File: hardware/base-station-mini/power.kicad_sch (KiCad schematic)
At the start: 28 parts, among them U2 TPS61023DRLR, U22 TPS22918DBVR, U9 TPS63020DSJR

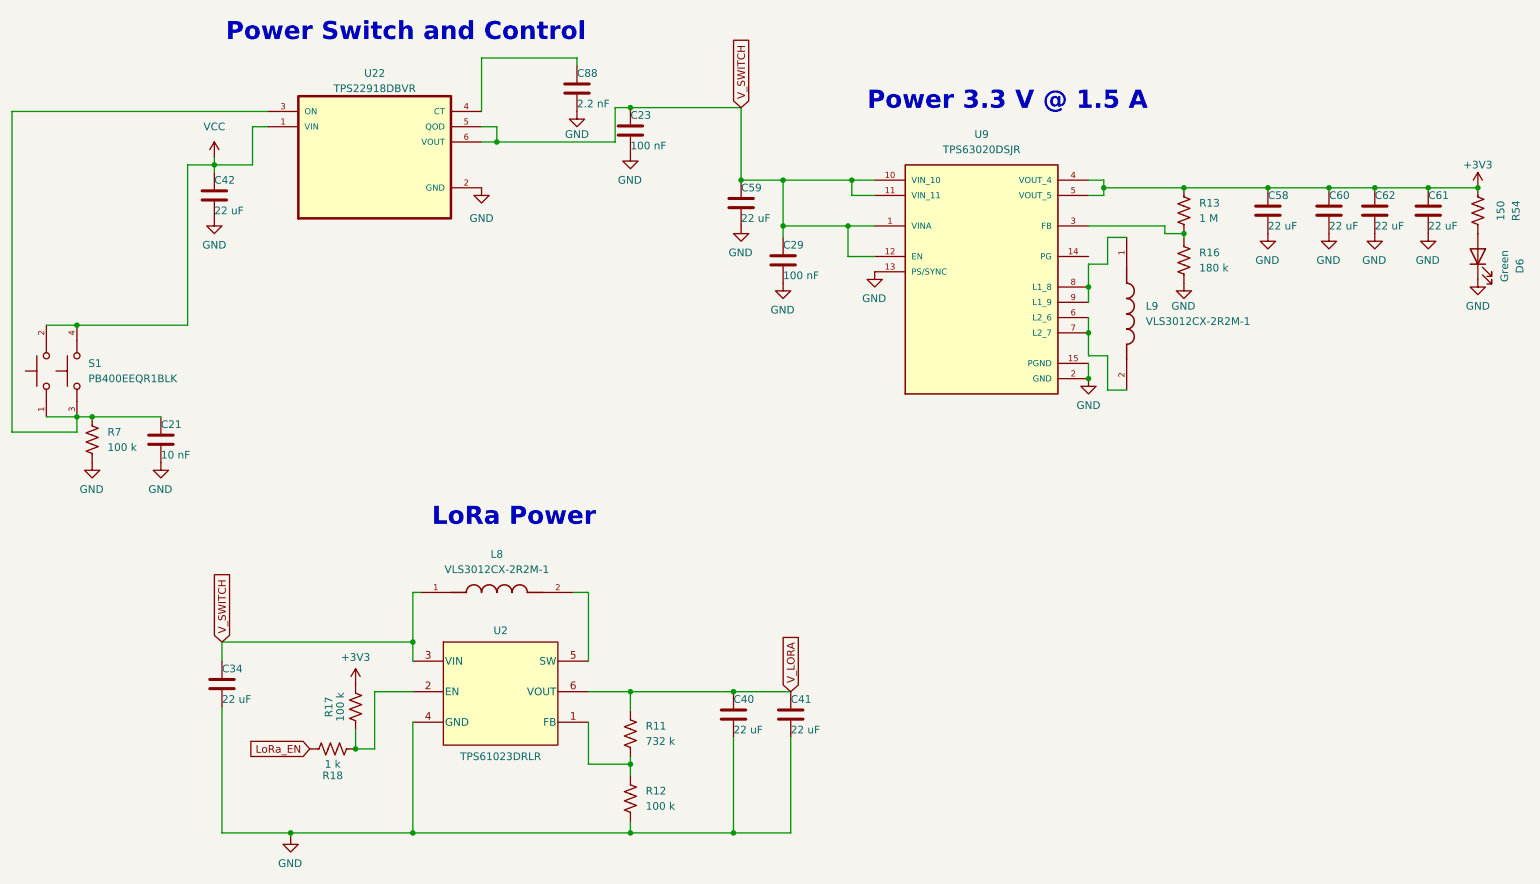
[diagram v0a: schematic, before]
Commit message: hardware: base-station-mini gains on-board LoRa, TPS63021, rev V1
Turns the fork into a reduced-feature ground station. "Mini" is fewer features,
not a smaller board -- the outline stays base-station's 30.27 x 90.50 mm.

RADIO. The E220-900MM22S (U16) is on-board on SPI, replacing the UART header
that fed an external lora-daughterboard. Eight ESP32 signals wired via the L_*
labels already placed on the module side; LoRa_TX/LoRa_RX/LoRa_EN were dangling
single-node stubs and their GPIOs went straight back into the radio bus.

All eight land on the same GPIOs as the fabbed lora-daughterboard -- SCK/17,
CS/18, MOSI/21, MISO/33, BUSY/34, RXEN/35, RST/38, DIO1/2 -- so the radio_board
firmware pin map applies unchanged. L_DI02 stays a module-local DIO2->TXEN loop,
so the SX1262 drives its own RF switch and spends no GPIO.

POWER. +3V3 had no source at all after the converters came out. Now a
fixed-output TPS63021 with FB tied to VOUT, matching base-station at V6. The 5 V
V_LORA boost stays deleted -- the on-board module runs off +3V3.

RF. J8 is new copper that exists on no other board. The feed was 0.20 mm, right
for a 0.1 mm prepreg but not for this stackup's real 0.2104 mm; it is now 0.36 mm
with a 0.15 mm coplanar gap, the value base-station's S7 derived for the same
JLCPCB JLC04161H-7628 stack. Net-(U16-ANT) was also missing from the RF netclass
-- the only RF net unique to this board was the one net not declared as RF -- so
it is added and the zones refilled.

ALSO. BT2 placed on B.Cu at base-station's exact coordinates, verified pad for
pad. external_charger.kicad_sch deleted rather than left orphaned; it held the
last copies of SDA_SENS, SCL_SENS, PosADC, MidADC and 25 dead symbols. Rev V1,
never fabbed. bom.csv regenerated -- it was 109 refs against a 78-ref schematic
and had never listed U16 or J8.

State: 0 schematic-parity issues, 0 unconnected, 25 DRC all silkscreen.
Reviewed in prefab-review-2026-08-12.md; three items open before fab, none
blockers.

Co-Auth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
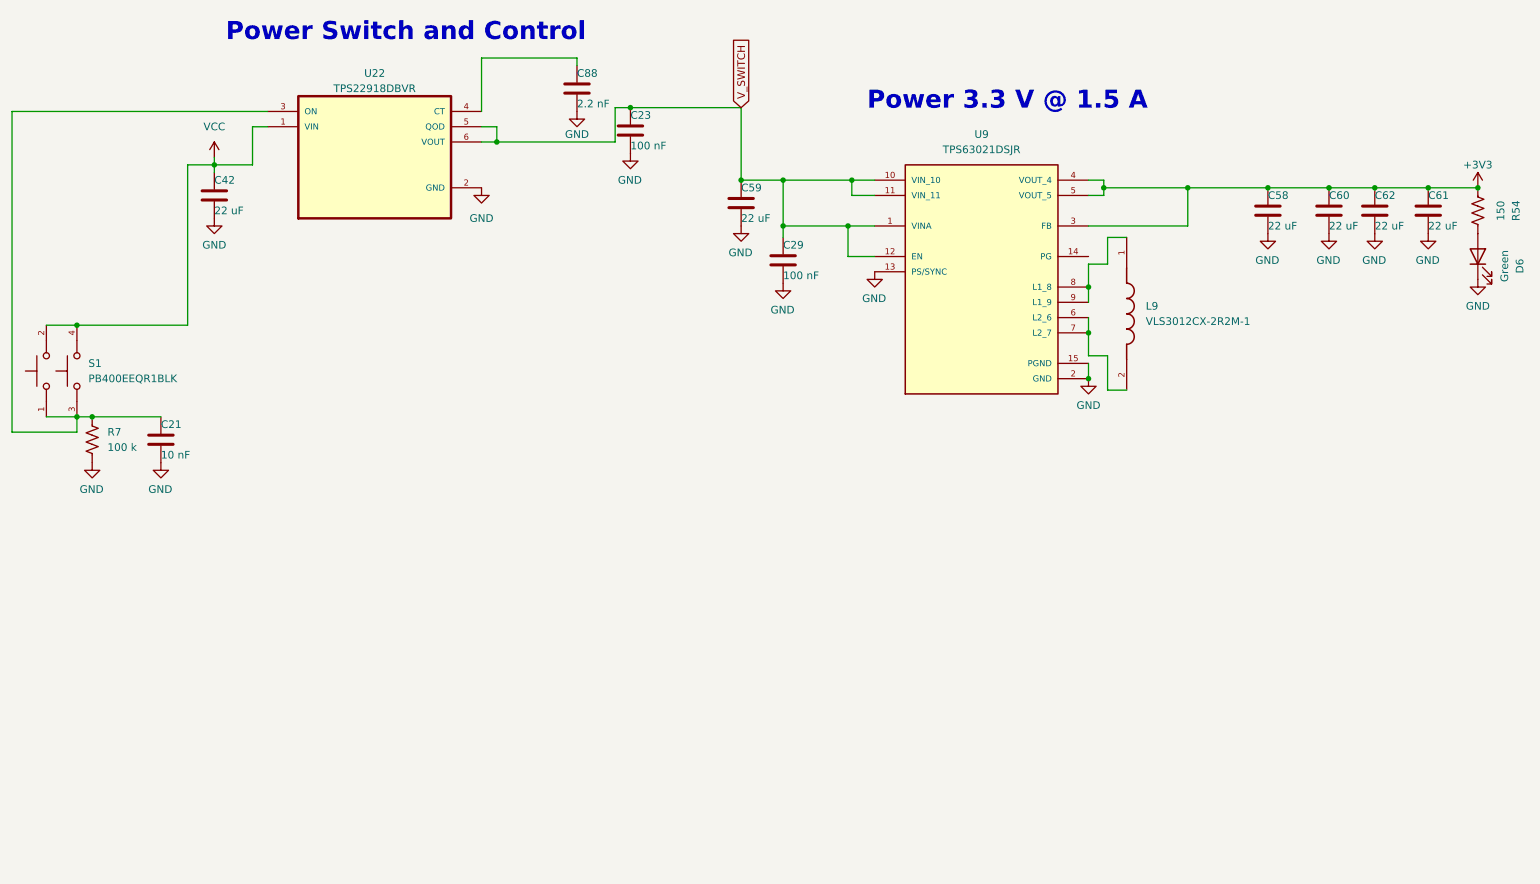
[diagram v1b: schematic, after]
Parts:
- removed C34, C40, C41: 22 uF, Capacitor_SMD:C_0805_2012Metric, symbol Device:C
- removed L8: VLS3012CX-2R2M-1, Footprints:IND_VLS3012CX-2R2M-1, symbol Custom:VLS3012CX-2R2M-1
- removed R11: 732 k, Resistor_SMD:R_0402_1005Metric, symbol Device:R_US
- removed R12, R17: 100 k, Resistor_SMD:R_0402_1005Metric, symbol Device:R_US
- removed R13: 1 M, Resistor_SMD:R_0402_1005Metric, symbol Device:R_US
- removed R16: 180 k, Resistor_SMD:R_0402_1005Metric, symbol Device:R_US
- removed R18: 1 k, Resistor_SMD:R_0402_1005Metric, symbol Device:R_US
- removed U2: TPS61023DRLR, Footprints:DRL0006A, symbol Custom:TPS61023DRLR
- U9: value TPS63020DSJR -> TPS63021DSJR; MP TPS63020DSJR -> TPS63021DSJR; MPN TPS63020DSJR -> TPS63021DSJR
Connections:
- net +3V3: now also U9.3 (FB)
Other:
- note removed: "LoRa Power"

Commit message: hardware(minis): cost-reduction part swaps (Tier A + USB-C + QMC5883P)
rocket-computer-mini:
- pyro high-side P-FETs U6-U10: TPN4R712MD -> Winsok WSD20L50DN33 (incumbent
  unbuyable at build qty until the Q4-2026 Mouser restock; land compatibility
  closed by numeric overlay of the vendor package drawing vs the TSON Advance
  land vs the Toshiba outline -- identical 0.202 mm bottom-metal overlap;
  first-article gate: end-face wetting + bench-fire)
- pyro-ARM N-FET U9: CSD16323Q3 -> AOS AON7534 (same pinout, land verified)
- gate drivers Q3-Q6: DTC123JEBTL -> DTC123JETL (SOT-416 leads land fully)
- battery shunt R72: CSSH0805FT2L00 -> Yageo PA0805FRF870R002L
- magnetometer U3: IIS2MDC -> QST QMC5883P (new Custom symbol + LGA-16 3x3
  footprint from the vendor land; U3 relocated, C2/C4/C6 re-arranged; C6
  220 nF -> 4.7 uF 16 V 0603 for the C1 reservoir; 2x2 mm all-layer no-pour
  rule area under the die; stale X/Y axis silk removed -- new markings when
  the firmware axis mapping is decided; needs a new ~10-register driver)
- USB-C stays GCT: the HRO's through-hole shell legs land inside the pyro
  terminal's back-side SMD pads -- physically blocked at this location

base-station-mini:
- USB-C J2: GCT USB4110-GF-A -> HRO TYPE-C-31-M-12 (project footprint with
  symbol-matched pad names; NPTH-aligned placement, mating face within
  0.03 mm of the GCT; R14/R15 nudged 1.0 mm, one GND via moved, VBUS
  re-bridged; DRC 0 unconnected / 0 parity; shell-leg holes must be fully
  filled with solder at assembly)
- thermistor TH1: 103AT-2 -> MF52B 103F3435-100 (beta 3435 matched, charger
  TS window unchanged)
- LEDs D6/D9: Kingbright -> Xinglight

both minis:
- 22 uF 0805: CL21A226MOQNNNE -> CL21A226KOQNNNE (tighter K tolerance)
- bom.csv regenerated from the schematics; TSON footprint tags updated

Verification: rocket-mini ERC one error better than baseline, DRC 246
unconnected (3 better), parity equal, no new errors; base-mini ERC unchanged,
DRC clean.

Co-Authored-By: Cla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
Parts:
- C42, C58, C59, C60, C61, C62: MPN CL21A226MOQNNNE -> CL21A226KOQNNNE
- D6: MPN WP710A10GD -> XL-302SYGD; Mfr Kingbright -> Xinglight
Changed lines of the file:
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@@
 			)
 		)
-		(property "MPN" "CL21A226MOQNNNE"
+		(property "MPN" "CL21A226KOQNNNE"
 			(at 241.3 48.26 0)
 			(hide yes)
@@
 			)
 		)
-		(property "MPN" "CL21A226MOQNNNE"
+		(property "MPN" "CL21A226KOQNNNE"
 			(at 250.19 48.26 0)
 			(hide yes)
@@
 			)
 		)
-		(property "MPN" "WP710A10GD"
+		(property "MPN" "XL-302SYGD"
 			(at 258.445 55.88 0)
 			(hide yes)
@@
 			)
 		)
-		(property "Mfr" "Kingbright"
+		(property "Mfr" "Xinglight"
 			(at 258.445 55.88 0)
 			(hide yes)
@@
 			)
 		)
-		(property "MPN" "CL21A226MOQNNNE"
+		(property "MPN" "CL21A226KOQNNNE"
 			(at 135.89 46.99 0)
 			(hide yes)
@@
 			)
 		)
-		(property "MPN" "CL21A226MOQNNNE"
+		(property "MPN" "CL21A226KOQNNNE"
 			(at 223.52 48.26 0)
 			(hide yes)
@@
 			)
 		)
-		(property "MPN" "CL21A226MOQNNNE"
+		(property "MPN" "CL21A226KOQNNNE"
 			(at 48.26 45.72 0)
 			(hide yes)
@@
 			)
 		)
-		(property "MPN" "CL21A226MOQNNNE"
+		(property "MPN" "CL21A226KOQNNNE"
 			(at 233.68 48.26 0)
 			(hide yes)

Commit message: hardware(base-station-mini): back to adjustable TPS63020 + FB divider
Applies the settled 2026-08-14 buck-boost decision that never landed in a
commit: U9 returns from the fixed-output TPS63021DSJR to the adjustable
TPS63020DSJR with its external divider, matching the full-size design intent
(the full-size base-station V6 still carries the 63021 and is NOT touched
here).

- new TPS63020DSJR symbol in the shared Custom lib (pin-identical clone of
  the 63021; only FB usage differs)
- FB-to-VOUT tie removed; divider added: R13 1M (VOUT->FB), R16 180k
  (FB->GND) -> VFB 0.5 V x (1 + 1M/180k) = 3.28 V
- junction added where R13 pin 1 meets the +3V3 wire (mid-wire pin)
- PCB: FB tie tracks removed (redundant inside the local +3V3 pour), R13/R16
  placed below U9 with FB routed to pin 3; placements are functional-first,
  fine-tune at layout review
- bom.csv regenerated; netlist verifies Net-(U9-FB) = U9.3 + R13.2 + R16.1

Never mix the two configurations: a divider on a 63021 drives ~21 V; a bare
FB tie on a 63020 pins the rail at the floor.

DRC: 0 unconnected, 0 parity, no new errors.

Co-Authored-By: Claude Fable 5 <noreply@anthropic.com>
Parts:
- added R13: 1 M, Resistor_SMD:R_0402_1005Metric, symbol Device:R_US
- added R16: 180 k, Resistor_SMD:R_0402_1005Metric, symbol Device:R_US
- U9: value TPS63021DSJR -> TPS63020DSJR; symbol Custom:TPS63021DSJR -> Custom:TPS63020DSJR; DigiKey_Part_Number 296-27259-1-ND -> (none); MPN TPS63021DSJR -> TPS63020DSJR
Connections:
- net +3V3: now also R13.1; no longer U9.3 (FB)
- net GND: now also R16.2
- new net: R13.2, R16.1, U9.3 (FB)

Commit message: hardware(base-mini): the 22 uF 0805 follows the fleet back to the M-code
The last board still carrying the retired K grade. #1454 (V10) and #1455
(rocket-mini) moved the other two after the priced CrossBoard BOM retired the
CL21A226KOQNNNE line on 2026-08-28 — it had repriced up to $0.1257@2000 against
the M-code's $0.0725 — and merged both minis back onto the M part. The sheet has
billed this board on the M line ever since; only its schematic still said K.

All seven placements (C20, C42, C58, C59, C60, C61, C62) move to
CL21A226MOQNNNE across the two sheets that carry them, the board's fields, and
bom.csv. Same Samsung series, same 0805, same 16 V.

That is the whole fleet on one 22 uF 0805 line again: rocket-computer 12,
rocket-computer-mini 14, base-station 12, base-station-mini 7,
lora-daughterboard 8.

Measured: field-only. Netlist unchanged at 80 components and 91 nets.
kicad-cli sch erc --severity-all unchanged at 402. kicad-cli pcb drc
--severity-all --schematic-parity unchanged at 49. bom.csv reconciles to the
schematic. check_docs.py clean.

Co-Authored-By: Claude Opus 5 <noreply@anthropic.com>
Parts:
- C42, C58, C59, C60, C61, C62: MPN CL21A226KOQNNNE -> CL21A226MOQNNNE
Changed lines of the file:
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@@
 			)
 		)
-		(property "MPN" "CL21A226KOQNNNE"
+		(property "MPN" "CL21A226MOQNNNE"
 			(at 241.3 48.26 0)
 			(hide yes)
@@
 			)
 		)
-		(property "MPN" "CL21A226KOQNNNE"
+		(property "MPN" "CL21A226MOQNNNE"
 			(at 250.19 48.26 0)
 			(hide yes)
@@
 			)
 		)
-		(property "MPN" "CL21A226KOQNNNE"
+		(property "MPN" "CL21A226MOQNNNE"
 			(at 135.89 46.99 0)
 			(hide yes)
@@
 			)
 		)
-		(property "MPN" "CL21A226KOQNNNE"
+		(property "MPN" "CL21A226MOQNNNE"
 			(at 223.52 48.26 0)
 			(hide yes)
@@
 			)
 		)
-		(property "MPN" "CL21A226KOQNNNE"
+		(property "MPN" "CL21A226MOQNNNE"
 			(at 48.26 45.72 0)
 			(hide yes)
@@
 			)
 		)
-		(property "MPN" "CL21A226KOQNNNE"
+		(property "MPN" "CL21A226MOQNNNE"
 			(at 233.68 48.26 0)
 			(hide yes)
